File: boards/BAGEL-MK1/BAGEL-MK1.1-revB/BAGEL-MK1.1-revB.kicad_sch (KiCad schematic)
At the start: 39 parts, among them J101 Conn_01x03, J102 Conn_01x04, J103 Conn_01x02, J104 Conn_01x02, J105 Conn_01x02, J106 Conn_01x04, U101 W25Q16JLUX, U102 STM32WB1MMC, U103 TPS7A25, U104 TCAL9538, U105 TCAL9538

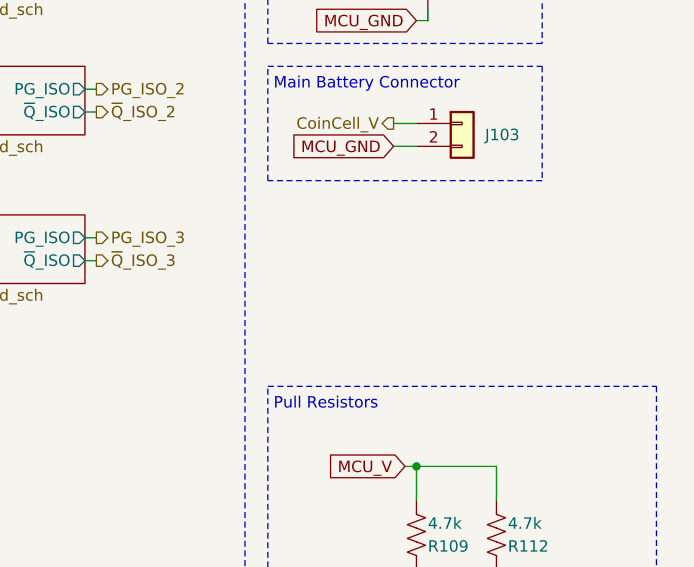
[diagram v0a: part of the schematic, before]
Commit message: constraint mounting hole & center hole courtyard
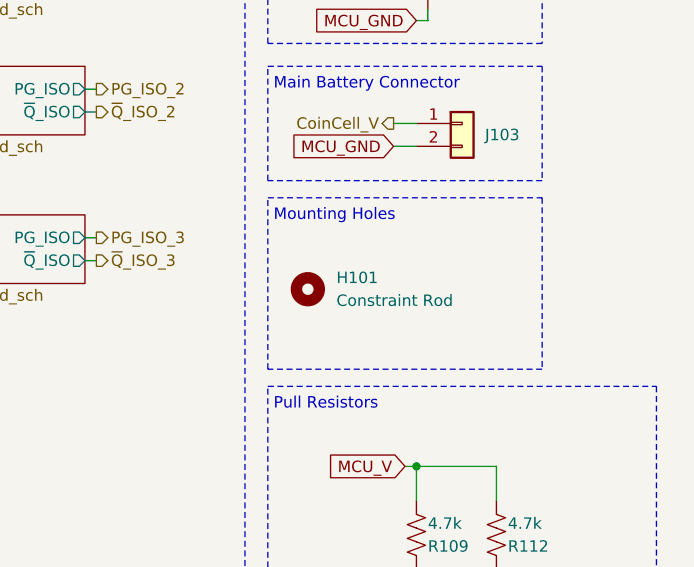
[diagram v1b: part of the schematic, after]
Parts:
- added H101: Constraint Rod, MountingHole:MountingHole_4.3mm_M4_Pad_Via, symbol Mechanical:MountingHole
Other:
- note added: "Mounting Holes"
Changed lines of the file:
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@@
 	)
 	(rectangle
+		(start 238.76 60.325)
+		(end 269.24 79.375)
+		(stroke
+			(width 0)
+			(type dash)
+		)
+		(fill
+			(type none)
+		)
+	)
+	(rectangle
 		(start 88.9 76.2)
 		(end 160.02 134.62)
@@
 		)
 	)
+	(text "Mounting Holes\n"
+		(exclude_from_sim no)
+		(at 239.395 61.595 0)
+		(effects
+			(font
+				(size 1.27 1.27)
+			)
+			(justify left top)
+		)
+	)
 	(text "Voltage Regulator"
 		(exclude_from_sim no)
@@
 					(unit 1)
 				)
+			)
+		)
+	)
+	(symbol
+		(lib_id "Mechanical:MountingHole")
+		(at 243.205 70.485 0)
+		(unit 1)
+		(exclude_from_sim no)
+		(in_bom no)
+		(on_board yes)
+		(dnp no)
+		(fields_autoplaced yes)
+		(property "Reference" "H101"
+			(at 246.38 69.2149 0)
+			(effects
+				(font
+					(size 1.27 1.27)
+				)
+				(justify left)
+			)
+		)
+		(property "Value" "Constraint Rod"
+			(at 246.38 71.7549 0)
+			(effects
+				(font
+					(size 1.27 1.27)
+				)
+				(justify left)
+			)
+		)
+		(property "Footprint" "MountingHole:MountingHole_4.3mm_M4_Pad_Via"
+			(at 243.205 70.485 0)
+			(effects
+				(font
+					(size 1.27 1.27)
+				)
+				(hide yes)
+			)
+		)
+		(property "Datasheet" "~"
+			(at 243.205 70.485 0)
+			(effects
+				(font
+					(size 1.27 1.27)
+				)
+				(hide yes)
+			)
+		)
+		(property "Description" "Mounting Hole without connection"
+			(at 243.205 70.485 0)
+			(effects
+				(font
+					(size 1.27 1.27)
+				)
+				(hide yes)
+			)
+		)
+		(instances
+			(project ""
+				(path "/27fcebe4-2fb8-4847-92ca-f98a7b250261"
+					(reference "H101")
+					(unit 1)
+				)

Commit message: lots of routing
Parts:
- removed H101: Constraint Rod, MountingHole:MountingHole_4.3mm_M4_Pad_Via, symbol Mechanical:MountingHole
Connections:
- net PG_ISO_4 is gone; now on net MCU_GND: U105.7 (P4)
- net PG_ISO_5 is gone; now on net MCU_GND: U105.3 (P1)
- net PG_ISO_6 is gone; now on net MCU_GND: U102.9 (PA4)
- net ~{Q}_ISO_4 is gone; now on net MCU_GND: U105.5 (P3)
- net ~{Q}_ISO_5 is gone; now on net MCU_GND: U105.4 (P2)
- net ~{Q}_ISO_6 is gone; now on net MCU_GND: U102.14 (PB8)
- no-connect marks 7 -> 9
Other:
- note added: "Disconnected Switches"
- note removed: "Mounting Holes"

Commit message: fixed voltage regulator symbol
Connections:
- net MCU_GND: now also U103.2 (NC)
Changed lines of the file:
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@@
 			)
 		)
-		(property "Datasheet" "https://www.ti.com/lit/ds/symlink/tps7a25.pdf?HQS=dis-dk-null-digikeymode-dsf-pf-null-wwe&ts=1768168918974"
+		(property "Datasheet" "https://product.torexsemi.com/system/files/series/xc6223.pdf"
 			(at 141.605 348.59 0)
 			(effects
@@
 			)
 		)
-		(property "Description" "300-mA, 18-V, Ultra-Low IQ, Low-Dropout Linear Voltage Regulator With Power-Good"
+		(property "Description" "300mA High Speed LDO Voltage Regulator"
 			(at 114.935 176.53 0)
 			(effects
@@
 		(pin "7"
 		)
+		(pin "2"
+		)
 		(instances
